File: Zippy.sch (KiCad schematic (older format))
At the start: 0 parts

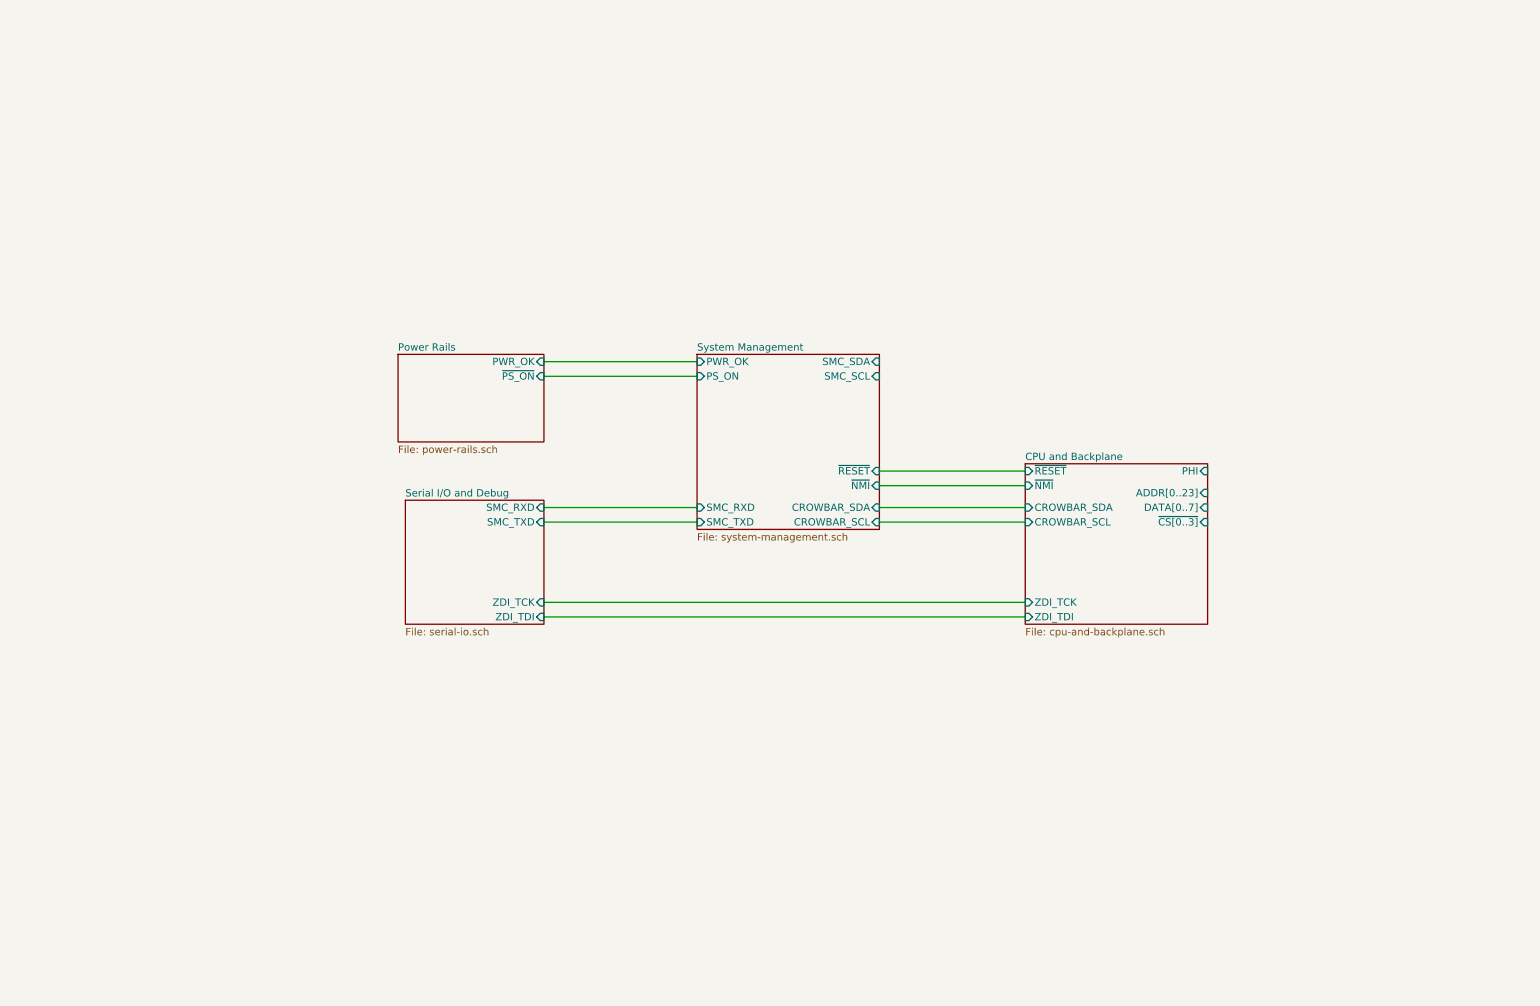
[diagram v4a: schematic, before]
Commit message: Cleanups and pruning
  - Migrated the Crowbar backplane out to the top level and
    promoted most of the signals to hierarchical labels.
  - Added a sheet for memory. Just a placeholder for now.
  - Wired up all the rest of the signals properly.
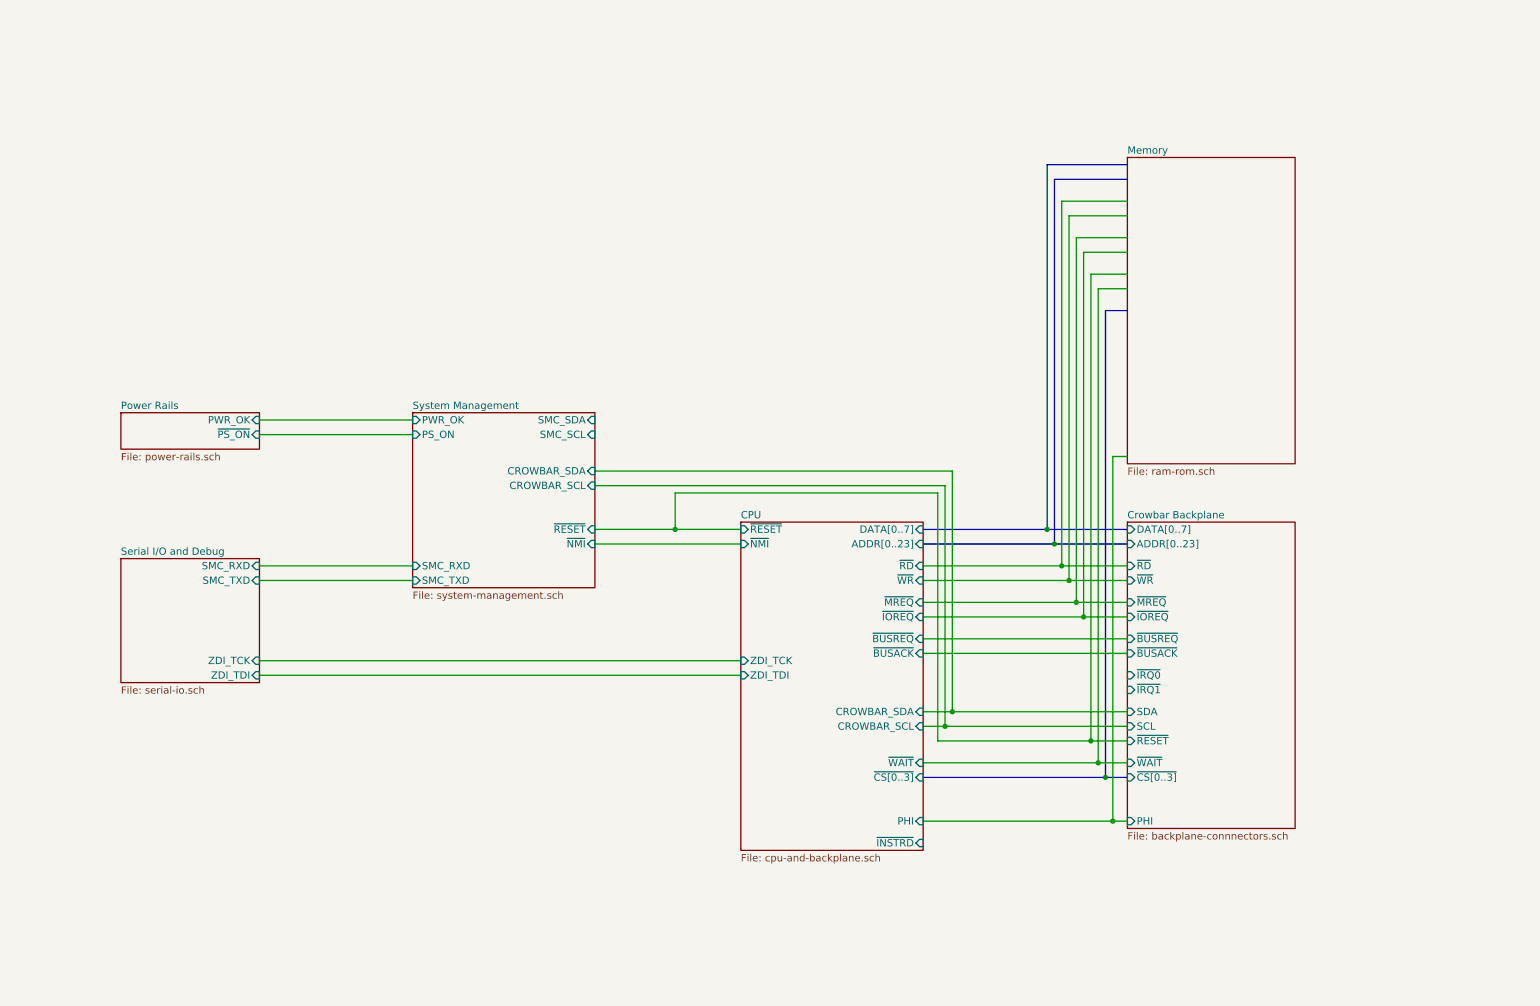
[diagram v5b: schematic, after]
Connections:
- wire segments 10 -> 50
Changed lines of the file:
@@
 $Descr A4 11693 8268
 encoding utf-8
-Sheet 1 6
+Sheet 1 7
 Title ""
 Date ""
@@
 $EndDescr
 $Sheet
-S 7600 3650 1250 1100
+S 5650 4050 1250 2250
 U 5D7F3F15
-F0 "CPU and Backplane" 50
+F0 "CPU" 50
 F1 "cpu-and-backplane.sch" 50
-F2 "~RESET" I L 7600 3700 50
-F3 "PHI" I R 8850 3700 50
-F4 "ADDR[0..23]" I R 8850 3850 50
-F5 "DATA[0..7]" I R 8850 3950 50
-F6 "~CS[0..3]" I R 8850 4050 50
-F7 "ZDI_TCK" I L 7600 4600 50
-F8 "ZDI_TDI" I L 7600 4700 50
-F9 "~NMI" I L 7600 3800 50
-F10 "CROWBAR_SCL" I L 7600 4050 50
-F11 "CROWBAR_SDA" I L 7600 3950 50
-$EndSheet
-$Sheet
-S 3300 2900 1000 600
+F2 "~RESET" I L 5650 4100 50
+F3 "PHI" I R 6900 6100 50
+F4 "ADDR[0..23]" I R 6900 4200 50
+F5 "DATA[0..7]" I R 6900 4100 50
+F6 "~CS[0..3]" I R 6900 5800 50
+F7 "ZDI_TCK" I L 5650 5000 50
+F8 "ZDI_TDI" I L 5650 5100 50
+F9 "~NMI" I L 5650 4200 50
+F10 "CROWBAR_SCL" I R 6900 5450 50
+F11 "CROWBAR_SDA" I R 6900 5350 50
+F12 "~IOREQ" I R 6900 4700 50
+F13 "~MREQ" I R 6900 4600 50
+F14 "~RD" I R 6900 4350 50
+F15 "~WR" I R 6900 4450 50
+F16 "~INSTRD" I R 6900 6250 50
+F17 "~WAIT" I R 6900 5700 50
+F18 "~BUSREQ" I R 6900 4850 50
+F19 "~BUSACK" I R 6900 4950 50
+$EndSheet
+$Sheet
+S 1400 3300 950  250
 U 5D86D88B
 F0 "Power Rails" 50
 F1 "power-rails.sch" 50
-F2 "PWR_OK" I R 4300 2950 50
-F3 "~PS_ON" I R 4300 3050 50
-$EndSheet
-$Sheet
-S 5350 2900 1250 1200
+F2 "PWR_OK" I R 2350 3350 50
+F3 "~PS_ON" I R 2350 3450 50
+$EndSheet
+Wire Wire Line
+	2350 3350 3400 3350
+Wire Wire Line
+	2350 3450 3400 3450
+Wire Wire Line
+	2350 4350 3400 4350
+Wire Wire Line
+	2350 4450 3400 4450
+$Sheet
+S 1400 4300 950  850
+U 5DA1EBE5
+F0 "Serial I/O and Debug" 50
+F1 "serial-io.sch" 50
+F2 "ZDI_TCK" I R 2350 5000 50
+F3 "ZDI_TDI" I R 2350 5100 50
+F4 "SMC_TXD" I R 2350 4450 50
+F5 "SMC_RXD" I R 2350 4350 50
+$EndSheet
+Wire Wire Line
+	2350 5000 5650 5000
+Wire Wire Line
+	2350 5100 5650 5100
+Wire Wire Line
+	4650 4100 5200 4100
+Wire Wire Line
+	4650 4200 5650 4200
+$Sheet
+S 8300 4050 1150 2100
+U 5D9D31F3
+F0 "Crowbar Backplane" 50
+F1 "backplane-connnectors.sch" 50
+F2 "DATA[0..7]" I L 8300 4100 50
+F3 "ADDR[0..23]" I L 8300 4200 50
+F4 "~RD" I L 8300 4350 50
+F5 "~WR" I L 8300 4450 50
+F6 "~MREQ" I L 8300 4600 50
+F7 "~IOREQ" I L 8300 4700 50
+F8 "~BUSREQ" I L 8300 4850 50
+F9 "~BUSACK" I L 8300 4950 50
+F10 "~IRQ0" I L 8300 5100 50
+F11 "~IRQ1" I L 8300 5200 50
+F12 "SDA" I L 8300 5350 50
+F13 "SCL" I L 8300 5450 50
+F14 "~WAIT" I L 8300 5700 50
+F15 "PHI" I L 8300 6100 50
+F16 "~RESET" I L 8300 5550 50
+F17 "~CS[0..3]" I L 8300 5800 50
+$EndSheet
+Wire Bus Line
+	6900 4100 7750 4100
+Wire Bus Line
+	6900 4200 7800 4200
+Wire Wire Line
+	6900 4350 7850 4350
+Wire Wire Line
+	6900 4450 7900 4450
+Wire Wire Line
+	6900 4600 7950 4600
+Wire Wire Line
+	6900 4700 8000 4700
+Wire Wire Line
+	6900 4850 8300 4850
+Wire Wire Line
+	6900 4950 8300 4950
+Wire Wire Line
+	6900 5350 7100 5350
+Wire Wire Line
+	6900 5450 7050 5450
+Wire Bus Line
+	6900 5800 8150 5800
+Wire Wire Line
+	6900 5700 8100 5700
+Wire Wire Line
+	7100 3700 7100 5350
+Wire Wire Line
+	4650 3700 7100 3700
+Connection ~ 7100 5350
+Wire Wire Line
+	7100 5350 8300 5350
+Wire Wire Line
+	7050 3800 7050 5450
+Wire Wire Line
+	4650 3800 7050 3800
+Connection ~ 7050 5450
+Wire Wire Line
+	7050 5450 8300 5450
+Wire Wire Line
+	5200 4100 5200 3850
+Wire Wire Line
+	5200 3850 7000 3850
+Wire Wire Line
+	7000 3850 7000 5550
+Wire Wire Line
+	7000 5550 8050 5550
+Connection ~ 5200 4100
+Wire Wire Line
+	5200 4100 5650 4100
+Wire Wire Line
+	6900 6100 8200 6100
+$Sheet
+S 3400 3300 1250 1200
 U 5D99435D
 F0 "System Management" 50
 F1 "system-management.sch" 50
-F2 "~RESET" I R 6600 3700 50
-F3 "PS_ON" I L 5350 3050 50
-F4 "SMC_RXD" I L 5350 3950 50
-F5 "SMC_TXD" I L 5350 4050 50
-F6 "CROWBAR_SDA" I R 6600 3950 50
-F7 "CROWBAR_SCL" I R 6600 4050 50
-F8 "~NMI" I R 6600 3800 50
-F9 "SMC_SDA" I R 6600 2950 50
-F10 "SMC_SCL" I R 6600 3050 50
-F11 "PWR_OK" I L 5350 2950 50
-$EndSheet
-Wire Wire Line
-	4300 2950 5350 2950
-Wire Wire Line
-	4300 3050 5350 3050
-Wire Wire Line
-	4300 3950 5350 3950
-Wire Wire Line
-	4300 4050 5350 4050
-$Sheet
-S 3350 3900 950  850
-U 5DA1EBE5
-F0 "Serial I/O and Debug" 50
-F1 "serial-io.sch" 50
-F2 "ZDI_TCK" I R 4300 4600 50
-F3 "ZDI_TDI" I R 4300 4700 50
-F4 "SMC_TXD" I R 4300 4050 50
-F5 "SMC_RXD" I R 4300 3950 50
-$EndSheet
-Wire Wire Line
-	4300 4600 7600 4600
-Wire Wire Line
-	4300 4700 7600 4700
-Wire Wire Line
-	6600 3700 7600 3700
-Wire Wire Line
-	6600 3800 7600 3800
-Wire Wire Line
-	6600 3950 7600 3950
-Wire Wire Line
-	6600 4050 7600 4050
+F2 "~RESET" I R 4650 4100 50
+F3 "PS_ON" I L 3400 3450 50
+F4 "SMC_RXD" I L 3400 4350 50
+F5 "SMC_TXD" I L 3400 4450 50
+F6 "CROWBAR_SDA" I R 4650 3700 50
+F7 "CROWBAR_SCL" I R 4650 3800 50
+F8 "~NMI" I R 4650 4200 50
+F9 "SMC_SDA" I R 4650 3350 50
+F10 "SMC_SCL" I R 4650 3450 50
+F11 "PWR_OK" I L 3400 3350 50
+$EndSheet
+$Sheet
+S 8300 1550 1150 2100
+U 5DCC6C4D
+F0 "Memory" 50
+F1 "ram-rom.sch" 50
+$EndSheet
+Wire Bus Line
+	7750 4100 7750 1600
+Wire Bus Line
+	7750 1600 8300 1600
+Connection ~ 7750 4100
+Wire Bus Line
+	7750 4100 8300 4100
+Wire Bus Line
+	7800 4200 7800 1700
+Wire Bus Line
+	7800 1700 8300 1700
+Connection ~ 7800 4200
+Wire Bus Line
+	7800 4200 8300 4200
+Wire Wire Line
+	7850 4350 7850 1850
+Wire Wire Line
+	7850 1850 8300 1850
+Connection ~ 7850 4350
+Wire Wire Line
+	7850 4350 8300 4350
+Wire Wire Line
+	7900 4450 7900 1950
+Wire Wire Line
+	7900 1950 8300 1950
+Connection ~ 7900 4450
+Wire Wire Line
+	7900 4450 8300 4450
+Wire Wire Line
+	7950 4600 7950 2100
+Wire Wire Line
+	7950 2100 8300 2100
+Connection ~ 7950 4600
+Wire Wire Line
+	7950 4600 8300 4600
+Wire Wire Line
+	8000 4700 8000 2200
+Wire Wire Line
+	8000 2200 8300 2200
+Connection ~ 8000 4700
+Wire Wire Line
+	8000 4700 8300 4700
+Wire Wire Line
+	8050 5550 8050 2350
+Wire Wire Line
+	8050 2350 8300 2350
+Connection ~ 8050 5550
+Wire Wire Line
+	8050 5550 8300 5550
+Wire Wire Line
+	8100 5700 8100 2450
+Wire Wire Line
+	8100 2450 8300 2450
+Connection ~ 8100 5700
+Wire Wire Line
+	8100 5700 8300 5700
+Wire Bus Line
+	8150 5800 8150 2600
+Wire Bus Line
+	8150 2600 8300 2600
+Connection ~ 8150 5800
+Wire Bus Line
+	8150 5800 8300 5800
+Wire Wire Line
+	8200 6100 8200 3600
+Wire Wire Line
+	8200 3600 8300 3600
+Connection ~ 8200 6100
+Wire Wire Line
+	8200 6100 8300 6100
 $EndSCHEMATC

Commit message: Addition of the main bus pins to the memory sheet.
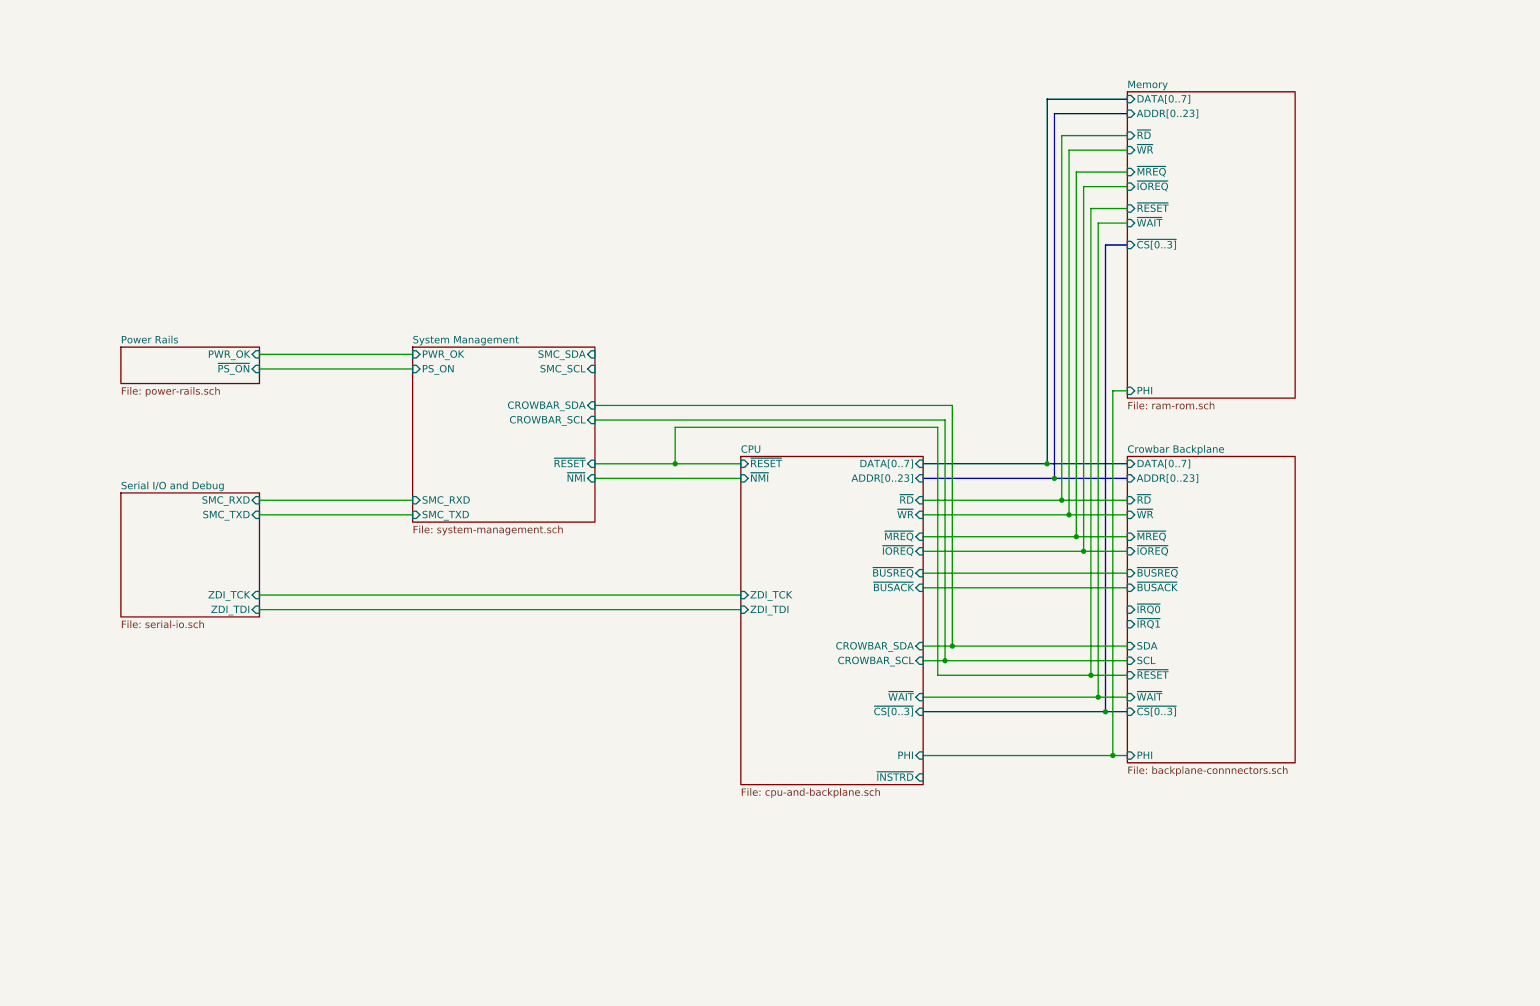
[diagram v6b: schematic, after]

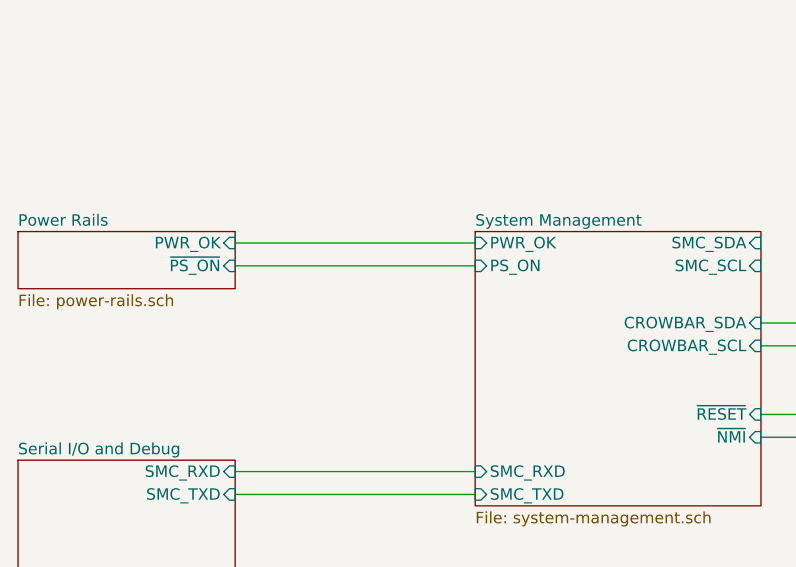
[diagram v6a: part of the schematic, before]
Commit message: Bookmark of where I'm at in the layout.
Last step for the serial debug interface is to route the RX/TX
lines through the opto-isolators and then to the eZ80 and the
supervisor uC.
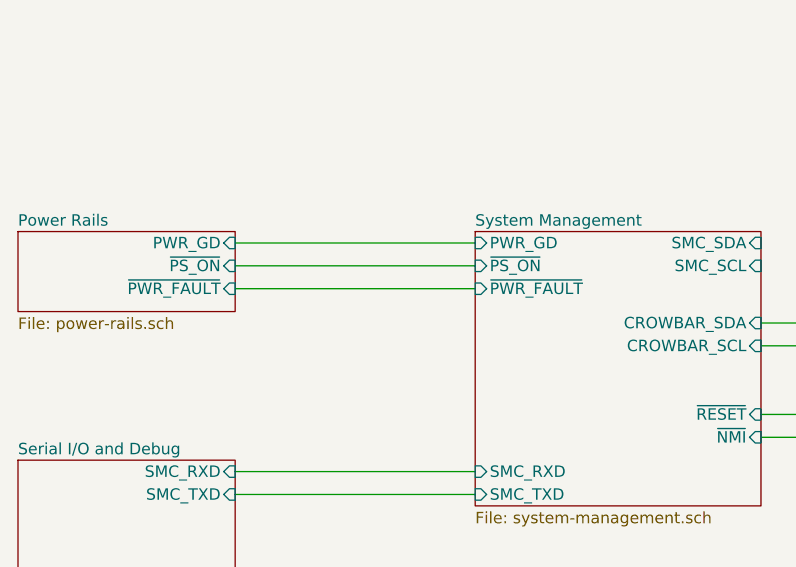
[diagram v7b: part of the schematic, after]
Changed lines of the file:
@@
 $EndSheet
 $Sheet
-S 1400 2850 950  250
+S 1400 2850 950  350
 U 5D86D88B
 F0 "Power Rails" 50
 F1 "power-rails.sch" 50
-F2 "PWR_OK" I R 2350 2900 50
-F3 "~PS_ON" I R 2350 3000 50
+F2 "~PS_ON" I R 2350 3000 50
+F3 "PWR_GD" I R 2350 2900 50
+F4 "~PWR_FAULT" I R 2350 3100 50
 $EndSheet
 Wire Wire Line
@@
 F1 "system-management.sch" 50
 F2 "~RESET" I R 4650 3650 50
-F3 "PS_ON" I L 3400 3000 50
-F4 "SMC_RXD" I L 3400 3900 50
-F5 "SMC_TXD" I L 3400 4000 50
-F6 "CROWBAR_SDA" I R 4650 3250 50
-F7 "CROWBAR_SCL" I R 4650 3350 50
-F8 "~NMI" I R 4650 3750 50
-F9 "SMC_SDA" I R 4650 2900 50
-F10 "SMC_SCL" I R 4650 3000 50
-F11 "PWR_OK" I L 3400 2900 50
+F3 "SMC_RXD" I L 3400 3900 50
+F4 "SMC_TXD" I L 3400 4000 50
+F5 "CROWBAR_SDA" I R 4650 3250 50
+F6 "CROWBAR_SCL" I R 4650 3350 50
+F7 "~NMI" I R 4650 3750 50
+F8 "SMC_SDA" I R 4650 2900 50
+F9 "SMC_SCL" I R 4650 3000 50
+F10 "~PS_ON" I L 3400 3000 50
+F11 "~PWR_FAULT" I L 3400 3100 50
+F12 "PWR_GD" I L 3400 2900 50
 $EndSheet
 $Sheet
@@
 Wire Wire Line
 	8200 5650 8300 5650
+Wire Wire Line
+	2350 3100 3400 3100
 $EndSCHEMATC
